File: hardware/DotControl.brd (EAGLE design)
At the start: 30.7 x 65 mm, 25 parts, among them CN1 1X4-BIG, J3 USB-MICROB, SW2 Previous, SW5 Previous, SW6 Next, SW8 Ok, U1 ATMEGA328P-MU-QFN32, U2 TMP102, U3 ATSHA204-TSU

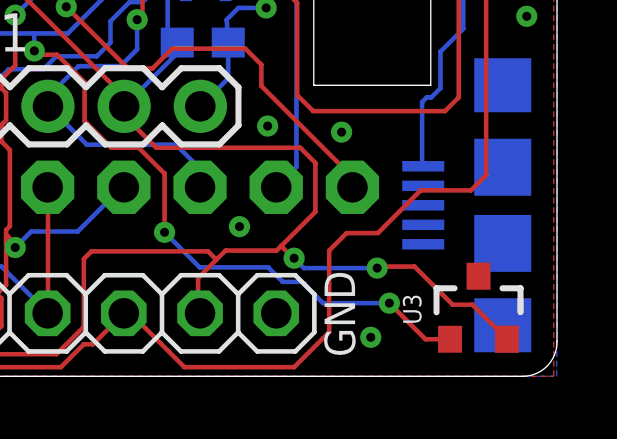
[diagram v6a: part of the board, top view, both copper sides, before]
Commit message: Reposition crypto module
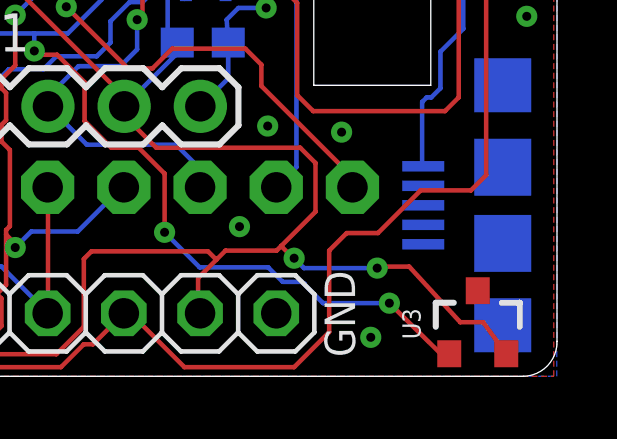
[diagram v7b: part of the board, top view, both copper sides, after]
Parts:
- moved U3 0.48 mm to (28.1, 1.75)
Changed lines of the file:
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@@
 <element name="U2" library="SparkFun" package="SOT563" value="TMP102" x="18.9992" y="13.1318" rot="MR270"/>
 <element name="C3" library="resistor" package="C0603" value="0.1uF" x="18.8976" y="11.1252" rot="MR180"/>
-<element name="U3" library="SparkFun-IC-Special-Function" package="SOT23-3" value="ATSHA204-TSU" x="28.0924" y="2.2352">
-<attribute name="PROD_ID" value="IC-11208" x="28.0924" y="3.2004" size="1.778" layer="27" display="off"/>
+<element name="U3" library="SparkFun-IC-Special-Function" package="SOT23-3" value="ATSHA204-TSU" x="28.067" y="1.7526">
+<attribute name="PROD_ID" value="IC-11208" x="28.067" y="2.7178" size="1.778" layer="27" display="off"/>
 </element>
 </elements>
@@
 <wire x1="21.9456" y1="3.937" x2="21.9202" y2="3.937" width="0.1524" layer="1"/>
 <wire x1="21.9202" y1="3.937" x2="21.5138" y2="4.3434" width="0.1524" layer="1"/>
-<wire x1="24.765" y1="3.6576" x2="25.9588" y2="3.6576" width="0.1524" layer="1"/>
-<wire x1="25.9588" y1="3.6576" x2="27.2288" y2="2.3876" width="0.1524" layer="1"/>
-<wire x1="27.2288" y1="2.3876" x2="27.89" y2="2.3876" width="0.1524" layer="1"/>
-<wire x1="27.89" y1="2.3876" x2="29.0424" y2="1.2352" width="0.1524" layer="1"/>
+<wire x1="24.765" y1="3.6576" x2="25.781" y2="3.6576" width="0.1524" layer="1"/>
+<wire x1="25.781" y1="3.6576" x2="27.4828" y2="1.8034" width="0.1524" layer="1"/>
+<wire x1="27.4828" y1="1.8034" x2="28.2456" y2="1.8034" width="0.1524" layer="1"/>
+<wire x1="28.2456" y1="1.8034" x2="29.017" y2="0.7526" width="0.1524" layer="1"/>
 </signal>
 <signal name="PUSH">
@@
 <via x="13.2842" y="10.8458" extent="1-16" drill="0.3"/>
 <wire x1="13.2842" y1="10.8458" x2="13.2842" y2="11.43" width="0.1524" layer="16"/>
-<wire x1="27.1424" y1="1.2352" x2="26.3238" y2="1.2352" width="0.1524" layer="1"/>
-<wire x1="26.3238" y1="1.2352" x2="25.1206" y2="2.4384" width="0.1524" layer="1"/>
+<wire x1="27.117" y1="0.7526" x2="26.8064" y2="0.778" width="0.1524" layer="1"/>
+<wire x1="26.8064" y1="0.778" x2="25.1206" y2="2.4384" width="0.1524" layer="1"/>
 </signal>
 <signal name="TXD">
